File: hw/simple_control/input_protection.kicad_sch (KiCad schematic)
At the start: 6 parts, among them Q1 AOSP21357

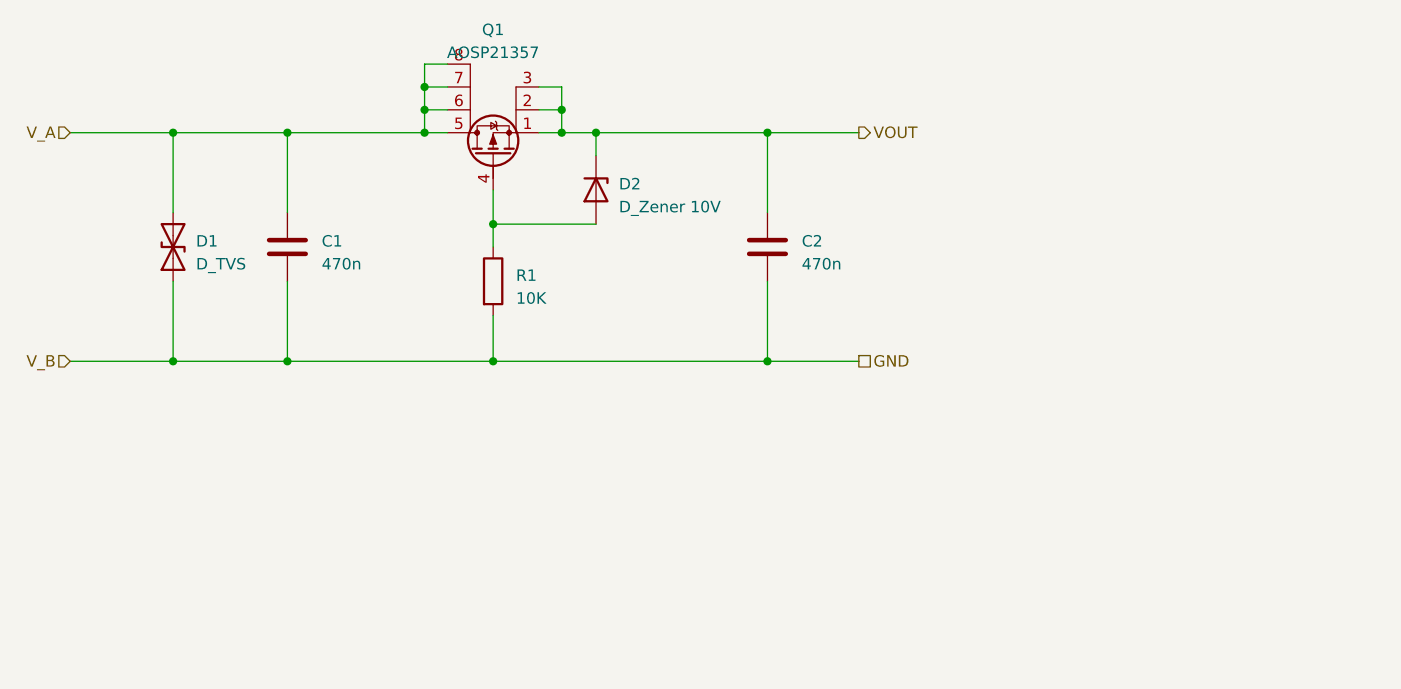
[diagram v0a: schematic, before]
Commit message: [hw] Add simple control LED driver
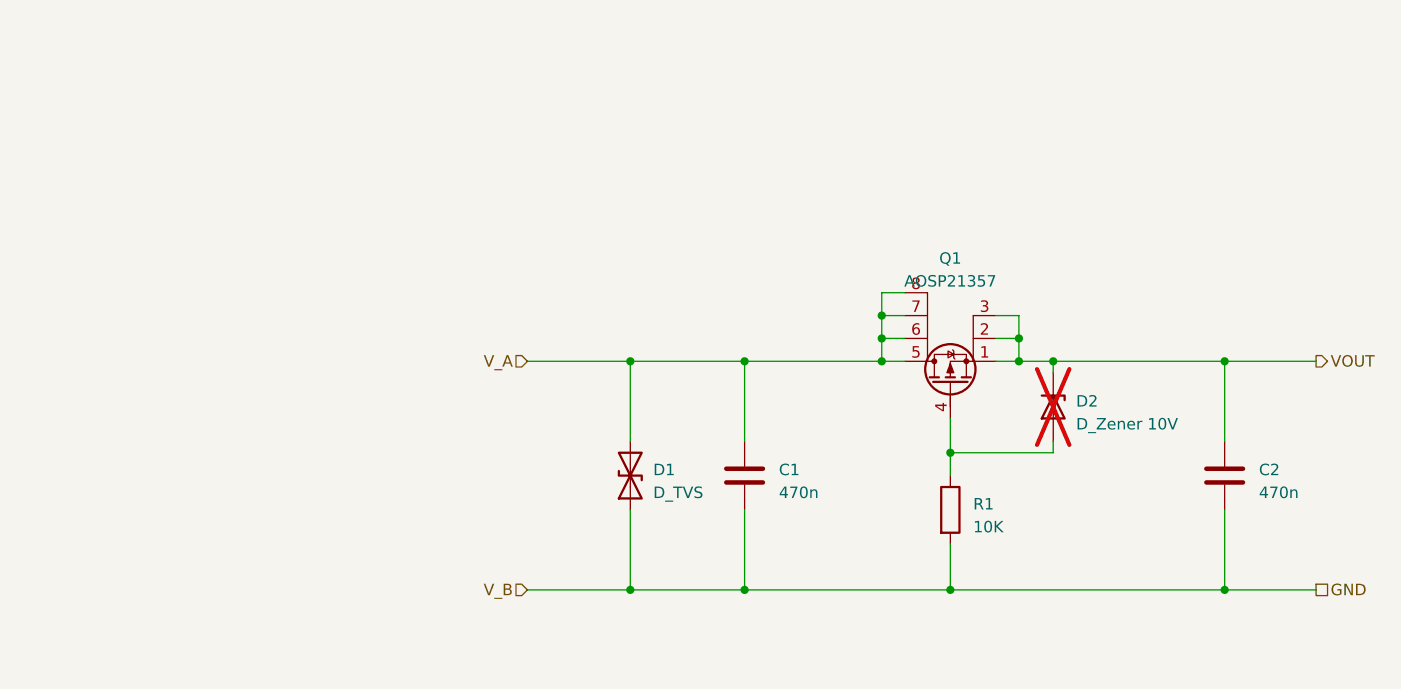
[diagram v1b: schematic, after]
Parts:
- D2: now not fitted; now left out of the parts list
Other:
- moved on the sheet: C1, C2, D1, Q1, R1

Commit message: [hw] Complete root schematics of simple control
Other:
- company: (none) -> Stefan Misik
- title: (none) -> WS2812 Simple Controller
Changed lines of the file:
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@@
 (kicad_sch (version 20230121) (generator eeschema)
   (paper "A4")
+  (title_block
+    (title "WS2812 Simple Controller")
+    (date "2023-03-09")
+    (company "Stefan Misik")
+    (comment 1 "Input Protection")
+  )
   (junction (at 114.3 88.9) (diameter 0) (color 0 0 0 0)
   )

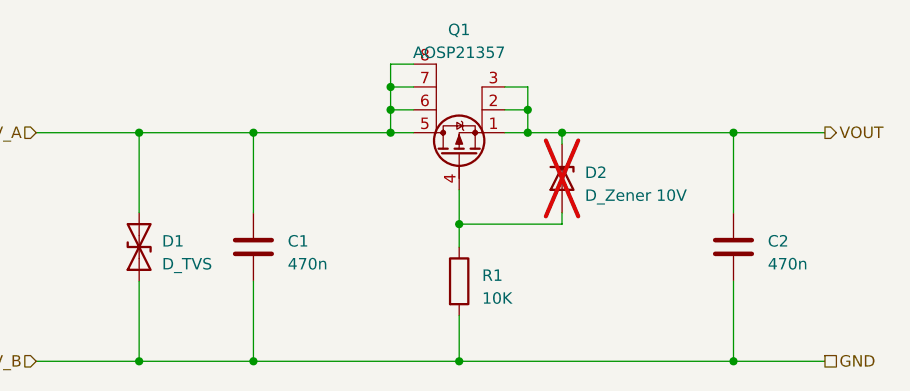
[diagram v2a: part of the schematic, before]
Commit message: [hw] Wire some RPi Pico/Zero connections
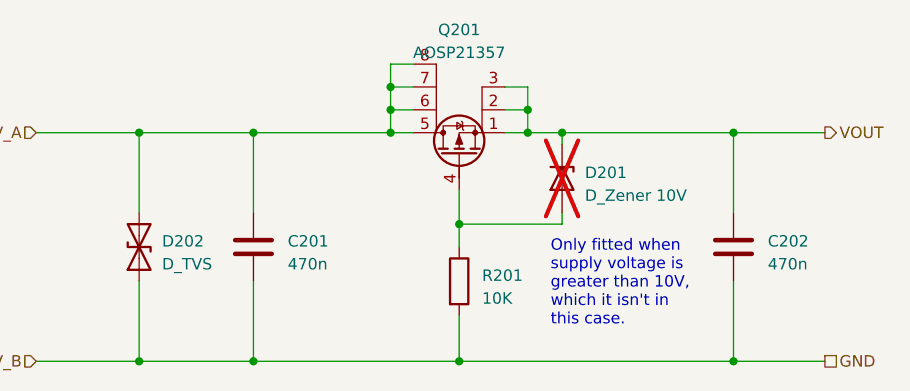
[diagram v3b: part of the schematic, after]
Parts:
- renumbered C1 to C201, C2 to C202, D2 to D201, D1 to D202, Q1 to Q201, R1 to R201
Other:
- note added: "Only fitted when supply voltage is greater than 10V, which it isn't in this case."
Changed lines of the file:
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@@
     (stroke (width 0) (type default))
+  )
+  (text "Only fitted when\nsupply voltage is\ngreater than 10V,\nwhich it isn't in\nthis case."
+    (at 147.32 110.49 0)
+    (effects (font (size 1.27 1.27)) (justify left bottom))
   )
   (hierarchical_label "VOUT" (shape output) (at 177.8 88.9 0) (fields_autoplaced)
@@
   (symbol (lib_id "Device:D_Zener") (at 148.59 93.98 270) (unit 1)
     (in_bom no) (on_board yes) (dnp yes) (fields_autoplaced)
-    (property "Reference" "D2" (at 151.13 93.345 90)
+    (property "Reference" "D201" (at 151.13 93.345 90)
       (effects (font (size 1.27 1.27)) (justify left))
     )
@@
       (project "simple_control"
         (path "/063164e8-0d2a-492b-8a61-e4fa4fbf06a6/9d1999f5-ea19-4a19-8c33-8b824114ea1f"
-          (reference "D2") (unit 1)
+          (reference "D201") (unit 1)
         )
       )
@@
   (symbol (lib_id "Device:C") (at 114.3 101.6 0) (unit 1)
     (in_bom yes) (on_board yes) (dnp no) (fields_autoplaced)
-    (property "Reference" "C1" (at 118.11 100.965 0)
+    (property "Reference" "C201" (at 118.11 100.965 0)
       (effects (font (size 1.27 1.27)) (justify left))
     )
@@
       (project "simple_control"
         (path "/063164e8-0d2a-492b-8a61-e4fa4fbf06a6/9d1999f5-ea19-4a19-8c33-8b824114ea1f"
-          (reference "C1") (unit 1)
+          (reference "C201") (unit 1)
         )
       )
@@
   (symbol (lib_id "Device:C") (at 167.64 101.6 0) (unit 1)
     (in_bom yes) (on_board yes) (dnp no) (fields_autoplaced)
-    (property "Reference" "C2" (at 171.45 100.965 0)
+    (property "Reference" "C202" (at 171.45 100.965 0)
       (effects (font (size 1.27 1.27)) (justify left))
     )
@@
       (project "simple_control"
         (path "/063164e8-0d2a-492b-8a61-e4fa4fbf06a6/9d1999f5-ea19-4a19-8c33-8b824114ea1f"
-          (reference "C2") (unit 1)
+          (reference "C202") (unit 1)
         )
       )
@@
   (symbol (lib_id "Device:R") (at 137.16 105.41 0) (unit 1)
     (in_bom yes) (on_board yes) (dnp no) (fields_autoplaced)
-    (property "Reference" "R1" (at 139.7 104.775 0)
+    (property "Reference" "R201" (at 139.7 104.775 0)
       (effects (font (size 1.27 1.27)) (justify left))
     )
@@
       (project "simple_control"
         (path "/063164e8-0d2a-492b-8a61-e4fa4fbf06a6/9d1999f5-ea19-4a19-8c33-8b824114ea1f"
-          (reference "R1") (unit 1)
+          (reference "R201") (unit 1)
         )
       )
@@
   (symbol (lib_id "my:Q_PMOS_SSSGDDDD") (at 137.16 91.44 90) (unit 1)
     (in_bom yes) (on_board yes) (dnp no) (fields_autoplaced)
-    (property "Reference" "Q1" (at 137.16 77.47 90)
+    (property "Reference" "Q201" (at 137.16 77.47 90)
       (effects (font (size 1.27 1.27)))
     )
@@
       (project "simple_control"
         (path "/063164e8-0d2a-492b-8a61-e4fa4fbf06a6/9d1999f5-ea19-4a19-8c33-8b824114ea1f"
-          (reference "Q1") (unit 1)
+          (reference "Q201") (unit 1)
         )
       )
@@
   (symbol (lib_id "Device:D_TVS") (at 101.6 101.6 90) (unit 1)
     (in_bom yes) (on_board yes) (dnp no) (fields_autoplaced)
-    (property "Reference" "D1" (at 104.14 100.965 90)
+    (property "Reference" "D202" (at 104.14 100.965 90)
       (effects (font (size 1.27 1.27)) (justify right))
     )
@@
       (project "simple_control"
         (path "/063164e8-0d2a-492b-8a61-e4fa4fbf06a6/9d1999f5-ea19-4a19-8c33-8b824114ea1f"
-          (reference "D1") (unit 1)
+          (reference "D202") (unit 1)
         )
       )

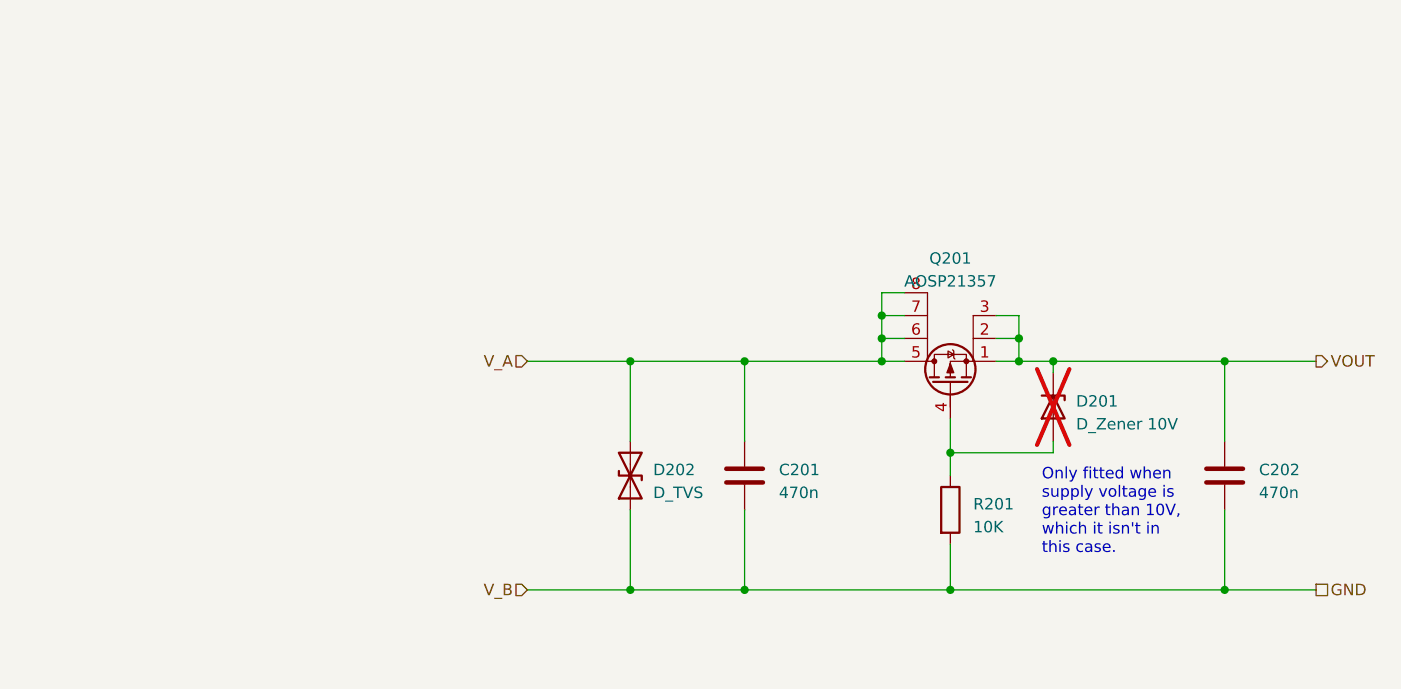
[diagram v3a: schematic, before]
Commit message: [hw] Fix ERC issues, update RPi Pico library
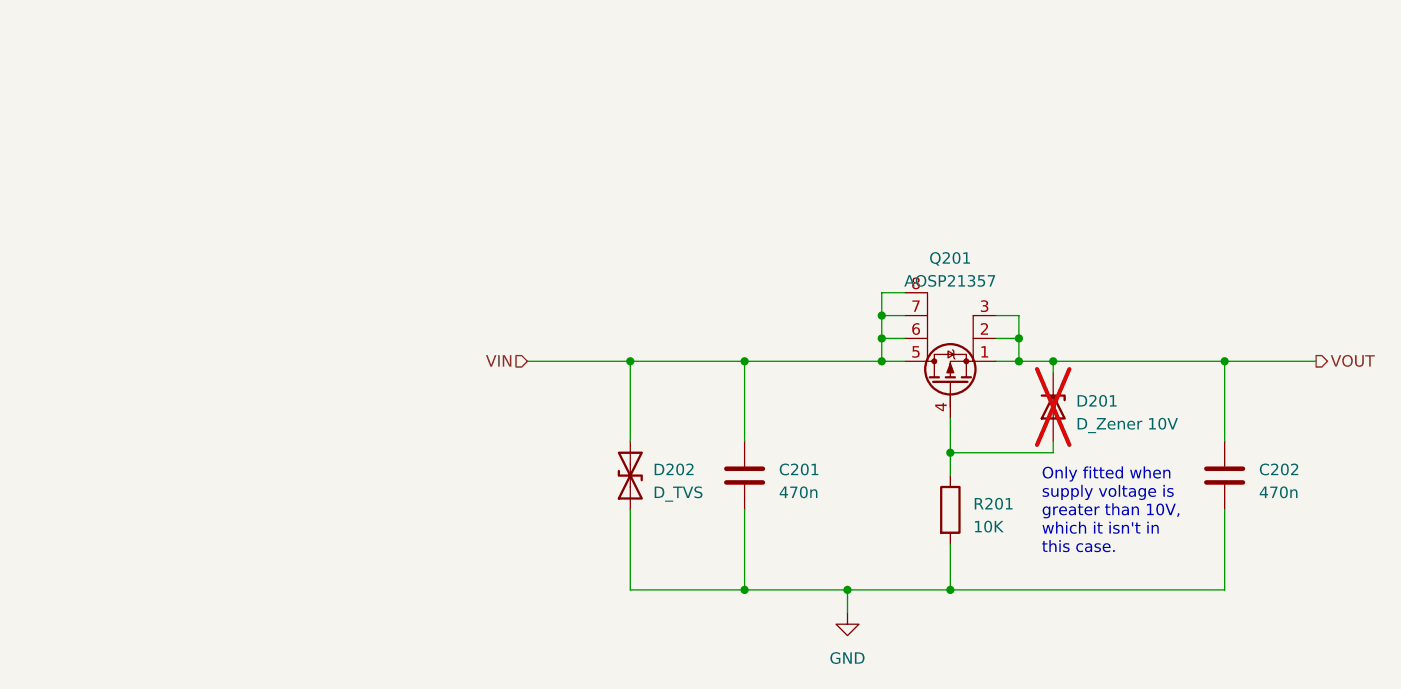
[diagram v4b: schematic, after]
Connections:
- net V_A renamed VIN
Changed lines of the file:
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@@
   (junction (at 114.3 114.3) (diameter 0) (color 0 0 0 0)
   )
-  (junction (at 167.64 114.3) (diameter 0) (color 0 0 0 0)
-  )
   (junction (at 144.78 88.9) (diameter 0) (color 0 0 0 0)
   )
@@
   (junction (at 144.78 86.36) (diameter 0) (color 0 0 0 0)
   )
+  (junction (at 125.73 114.3) (diameter 0) (color 0 0 0 0)
+  )
   (junction (at 167.64 88.9) (diameter 0) (color 0 0 0 0)
   )
-  (junction (at 101.6 114.3) (diameter 0) (color 0 0 0 0)
-  )
   (junction (at 137.16 114.3) (diameter 0) (color 0 0 0 0)
   )
@@
     (stroke (width 0) (type default))
   )
-  (wire (pts (xy 114.3 114.3) (xy 137.16 114.3))
+  (wire (pts (xy 114.3 114.3) (xy 125.73 114.3))
     (stroke (width 0) (type default))
   )
@@
     (stroke (width 0) (type default))
   )
-  (wire (pts (xy 167.64 114.3) (xy 177.8 114.3))
-    (stroke (width 0) (type default))
-  )
   (wire (pts (xy 90.17 88.9) (xy 101.6 88.9))
     (stroke (width 0) (type default))
@@
     (stroke (width 0) (type default))
   )
-  (wire (pts (xy 90.17 114.3) (xy 101.6 114.3))
-    (stroke (width 0) (type default))
-  )
   (wire (pts (xy 137.16 114.3) (xy 167.64 114.3))
     (stroke (width 0) (type default))
@@
     (stroke (width 0) (type default))
   )
+  (wire (pts (xy 125.73 114.3) (xy 137.16 114.3))
+    (stroke (width 0) (type default))
+  )
   (wire (pts (xy 148.59 97.79) (xy 148.59 99.06))
     (stroke (width 0) (type default))
@@
   )
   (wire (pts (xy 101.6 105.41) (xy 101.6 114.3))
+    (stroke (width 0) (type default))
+  )
+  (wire (pts (xy 125.73 114.3) (xy 125.73 116.84))
     (stroke (width 0) (type default))
   )
@@
     (effects (font (size 1.27 1.27)) (justify left))
   )
-  (hierarchical_label "V_A" (shape input) (at 90.17 88.9 180) (fields_autoplaced)
-    (effects (font (size 1.27 1.27)) (justify right))
-  )
-  (hierarchical_label "GND" (shape passive) (at 177.8 114.3 0) (fields_autoplaced)
-    (effects (font (size 1.27 1.27)) (justify left))
-  )
-  (hierarchical_label "V_B" (shape input) (at 90.17 114.3 180) (fields_autoplaced)
+  (hierarchical_label "VIN" (shape input) (at 90.17 88.9 180) (fields_autoplaced)
     (effects (font (size 1.27 1.27)) (justify right))
   )
@@
         )
       )
+    )
+  )
+  (symbol (lib_id "power:GND") (at 125.73 116.84 0) (unit 1)
+    (in_bom yes) (on_board yes) (dnp no) (fields_autoplaced)
+    (property "Reference" "#PWR0201" (at 125.73 123.19 0)
+      (effects (font (size 1.27 1.27)) hide)
+    )
+    (property "Value" "GND" (at 125.73 121.92 0)
+      (effects (font (size 1.27 1.27)))
+    )
+    (property "Footprint" "" (at 125.73 116.84 0)
+      (effects (font (size 1.27 1.27)) hide)
+    )
+    (property "Datasheet" "" (at 125.73 116.84 0)
+      (effects (font (size 1.27 1.27)) hide)
+    )
+    (pin "1")
+    (instances
+      (project "simple_control"
+        (path "/063164e8-0d2a-492b-8a61-e4fa4fbf06a6/9d1999f5-ea19-4a19-8c33-8b824114ea1f"
+          (reference "#PWR0201") (unit 1)
+        )
+      )

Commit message: chore(hw): assign footprints
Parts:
- C201, C202: footprint (none) -> Capacitor_SMD:C_0805_2012Metric_Pad1.18x1.45mm_HandSolder
- D201: footprint (none) -> Diode_SMD:D_MiniMELF_Handsoldering
- D202: footprint (none) -> Diode_SMD:D_SMB-SMC_Universal_Handsoldering
- Q201: footprint (none) -> Package_SO:SOIC-8_3.9x4.9mm_P1.27mm
- R201: footprint (none) -> Resistor_SMD:R_0805_2012Metric_Pad1.20x1.40mm_HandSolder
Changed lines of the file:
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@@
       (effects (font (size 1.27 1.27)) (justify left))
     )
-    (property "Footprint" "" (at 148.59 93.98 0)
+    (property "Footprint" "Diode_SMD:D_MiniMELF_Handsoldering" (at 148.59 93.98 0)
       (effects (font (size 1.27 1.27)) hide)
     )
@@
       (effects (font (size 1.27 1.27)) (justify left))
     )
-    (property "Footprint" "" (at 115.2652 105.41 0)
+    (property "Footprint" "Capacitor_SMD:C_0805_2012Metric_Pad1.18x1.45mm_HandSolder" (at 115.2652 105.41 0)
       (effects (font (size 1.27 1.27)) hide)
     )
@@
       (effects (font (size 1.27 1.27)) (justify left))
     )
-    (property "Footprint" "" (at 168.6052 105.41 0)
+    (property "Footprint" "Capacitor_SMD:C_0805_2012Metric_Pad1.18x1.45mm_HandSolder" (at 168.6052 105.41 0)
       (effects (font (size 1.27 1.27)) hide)
     )
@@
       (effects (font (size 1.27 1.27)) (justify left))
     )
-    (property "Footprint" "" (at 135.382 105.41 90)
+    (property "Footprint" "Resistor_SMD:R_0805_2012Metric_Pad1.20x1.40mm_HandSolder" (at 135.382 105.41 90)
       (effects (font (size 1.27 1.27)) hide)
     )
@@
       (effects (font (size 1.27 1.27)))
     )
-    (property "Footprint" "" (at 134.62 86.36 0)
+    (property "Footprint" "Package_SO:SOIC-8_3.9x4.9mm_P1.27mm" (at 134.62 86.36 0)
       (effects (font (size 1.27 1.27)) hide)
     )
@@
       (effects (font (size 1.27 1.27)) (justify right))
     )
-    (property "Footprint" "" (at 101.6 101.6 0)
+    (property "Footprint" "Diode_SMD:D_SMB-SMC_Universal_Handsoldering" (at 101.6 101.6 0)
       (effects (font (size 1.27 1.27)) hide)
     )

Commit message: chore(hw): swap SPI flash module for SD card
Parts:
- C201: footprint Capacitor_SMD:C_0805_2012Metric_Pad1.18x1.45mm_HandSolder -> Jumper:SolderJumper-2_P1.3mm_Open_RoundedPad1.0x1.5mm
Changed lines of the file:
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@@
       (effects (font (size 1.27 1.27)) (justify left))
     )
-    (property "Footprint" "Capacitor_SMD:C_0805_2012Metric_Pad1.18x1.45mm_HandSolder" (at 115.2652 105.41 0)
+    (property "Footprint" "Jumper:SolderJumper-2_P1.3mm_Open_RoundedPad1.0x1.5mm" (at 115.2652 105.41 0)
       (effects (font (size 1.27 1.27)) hide)
     )

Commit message: chore(hw): fix footprints
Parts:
- C201: footprint Jumper:SolderJumper-2_P1.3mm_Open_RoundedPad1.0x1.5mm -> Capacitor_SMD:C_0805_2012Metric_Pad1.18x1.45mm_HandSolder
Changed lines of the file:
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@@
       (effects (font (size 1.27 1.27)) (justify left))
     )
-    (property "Footprint" "Jumper:SolderJumper-2_P1.3mm_Open_RoundedPad1.0x1.5mm" (at 115.2652 105.41 0)
+    (property "Footprint" "Capacitor_SMD:C_0805_2012Metric_Pad1.18x1.45mm_HandSolder" (at 115.2652 105.41 0)
       (effects (font (size 1.27 1.27)) hide)
     )
